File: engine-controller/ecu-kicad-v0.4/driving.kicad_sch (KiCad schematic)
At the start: 94 parts, among them U1 MCP1416, U10 RQ3E100, U11 MCP1416, U12 RQ3E100, U13 MCP1416, U14 MCP1416, U15 RQ3E100, U16 RQ3E100, U17 MCP1416, U18 MCP1416, U19 MCP1416, U20 MCP1416, U21 RQ3E100, U22 RQ3E100, U23 RQ3E100, U24 RQ3E100, U25 MCP1416, U26 MCP1416, U27 RQ3E100, U28 RQ3E100, U29 MCP1416, U30 MCP1416, U4 MCP1416, U5 MCP1416, U51 RQ3E100, U52 MCP1416, U53 RQ3E100, U54 MCP1416, U55 RQ3E100, U56 MCP1416, U57 RQ3E100, U58 MCP1416, U6 RQ3E100, U7 MCP1416, U8 RQ3E100, U9 MCP1416

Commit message: That's a lot of changes
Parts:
- added C74, C75, C76, C77: 1uF, Capacitor_SMD:C_0402_1005Metric, symbol Device:C_Small
- added R57, R58, R59, R60: 20K, symbol Device:R_Small
- added U59, U60, U61, U62: MCP1416, Package_TO_SOT_SMD:SOT-23-5, symbol Driver_FET:MCP1416
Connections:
- net +5V: now also C74.2, C75.2, C76.2, C77.2, U59.2 (Vdd), U60.2 (Vdd), U61.2 (Vdd), U62.2 (Vdd)
- net GND: now also C74.1, C75.1, C76.1, C77.1, R57.1, R58.1, R59.1, R60.1, U59.4 (GND), U60.4 (GND), U61.4 (GND), U62.4 (GND)
- new net PWM_CTRL4: R57.2, U59.3 (IN)
- new net PWM_CTRL5: R58.2, U60.3 (IN)
- new net PWM_CTRL6: R59.2, U61.3 (IN)
- new net PWM_CTRL7: R60.2, U62.3 (IN)
- new net PWM_OUT4: U59.5 (OUT)
- new net PWM_OUT5: U60.5 (OUT)
- new net PWM_OUT6: U61.5 (OUT)
- new net PWM_OUT7: U62.5 (OUT)
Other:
- moved on the sheet: C1, C10, C11, C12, C13, C2, C3, C37, C38, C39, C4, C5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

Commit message: Changed ECU v0.4 to use more fused outputs
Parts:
- removed C11, C12, C13, C37, C72, C73: 1uF, Capacitor_SMD:C_0402_1005Metric, symbol Device:C_Small
- removed D10, D11, D12, D15, D16, D9: GS1G, Diode_SMD:D_SMA, symbol Device:D_Small
- removed R11, R12, R13, R14, R55, R56: 20K, symbol Device:R_Small
- removed U19, U20, U25, U26, U56, U58: MCP1416, Package_TO_SOT_SMD:SOT-23-5, symbol Driver_FET:MCP1416
- removed U23, U24, U27, U28, U55, U57: RQ3E100, CustomFootprints:HSMT-8, symbol CustomSymbols:RQ3E100
- added C94, C95, C96, C97, C98, C99: 1uF, Capacitor_SMD:C_0402_1005Metric, symbol Device:C_Small
- added D17, D18, D19, D20, D21, D22: GS1G, Diode_SMD:D_SMA, symbol Device:D_Small
- added F3, F4, F5, F6, F7, F8: SF-2410F-T, CustomFootprints:SF-2410F-T, symbol Device:Fuse_Small
- added R20, R39, R40, R48, R49, R50: 20K, symbol Device:R_Small
- added U34, U37, U47, U48, U49, U50: MCP1416, Package_TO_SOT_SMD:SOT-23-5, symbol Driver_FET:MCP1416
- added U38, U46, U63, U64, U65, U66: RQ3E100, CustomFootprints:HSMT-8, symbol CustomSymbols:RQ3E100
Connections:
- net +12V: now also C94.2, C95.2, C96.2, C97.2, C98.2, C99.2, U34.2 (Vdd), U37.2 (Vdd), U47.2 (Vdd), U48.2 (Vdd), U49.2 (Vdd), U50.2 (Vdd)
- net GND: now also C94.1, C95.1, C96.1, C97.1, C98.1, C99.1, R20.1, R39.1, R40.1, R48.1, R49.1, R50.1, U34.4 (GND), U37.4 (GND), U38.1 (Source), U38.2 (Source), U38.3 (Source), U46.1 (Source), U46.2 (Source), U46.3 (Source), U47.4 (GND), U48.4 (GND), U49.4 (GND), U50.4 (GND), U63.1 (Source), U63.2 (Source), U63.3 (Source), U64.1 (Source), U64.2 (Source), U64.3 (Source), U65.1 (Source), U65.2 (Source), U65.3 (Source), U66.1 (Source), U66.2 (Source), U66.3 (Source)
- net Vdrive: now also D17.1 (K), D18.1 (K), D19.1 (K), D20.1 (K), D21.1 (K), D22.1 (K)
- net OUT_AUX0 renamed OUT_FUSED0
- net OUT_AUX1 renamed OUT_FUSED1
- net OUT_AUX_CTRL0 renamed OUT_FUSED_CTRL0
- net OUT_AUX_CTRL1 renamed OUT_FUSED_CTRL1
- net OUT_FUSED_CTRL1: now also R20.2, U34.3 (IN)
- new net: F5.1, U63.5 (Drain), U63.6 (Drain), U63.7 (Drain), U63.8 (Drain)
- new net: U47.5 (OUT), U63.4 (Gate)
- new net: U34.5 (OUT), U38.4 (Gate)
- new net: F3.1, U38.5 (Drain), U38.6 (Drain), U38.7 (Drain), U38.8 (Drain)
- new net: U49.5 (OUT), U65.4 (Gate)
- new net: F7.1, U65.5 (Drain), U65.6 (Drain), U65.7 (Drain), U65.8 (Drain)
- new net: F6.1, U64.5 (Drain), U64.6 (Drain), U64.7 (Drain), U64.8 (Drain)
- new net: U48.5 (OUT), U64.4 (Gate)
- new net: U50.5 (OUT), U66.4 (Gate)
- new net: F8.1, U66.5 (Drain), U66.6 (Drain), U66.7 (Drain), U66.8 (Drain)
- new net: F4.1, U46.5 (Drain), U46.6 (Drain), U46.7 (Drain), U46.8 (Drain)
- new net: U37.5 (OUT), U46.4 (Gate)
- new net OUT_FUSED2: D17.2 (A), F3.2
- new net OUT_FUSED3: D18.2 (A), F4.2
- new net OUT_FUSED4: D19.2 (A), F5.2
- new net OUT_FUSED5: D20.2 (A), F6.2
- new net OUT_FUSED6: D21.2 (A), F7.2
- new net OUT_FUSED7: D22.2 (A), F8.2
- new net OUT_FUSED_CTRL3: R39.2, U37.3 (IN)
- new net OUT_FUSED_CTRL4: R40.2, U47.3 (IN)
- new net OUT_FUSED_CTRL5: R48.2, U48.3 (IN)
- new net OUT_FUSED_CTRL6: R49.2, U49.3 (IN)
- new net OUT_FUSED_CTRL7: R50.2, U50.3 (IN)
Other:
- moved on the sheet: C3, C4, D1, D2, F1, F2, R3, R4, U5, U6, U7, U8

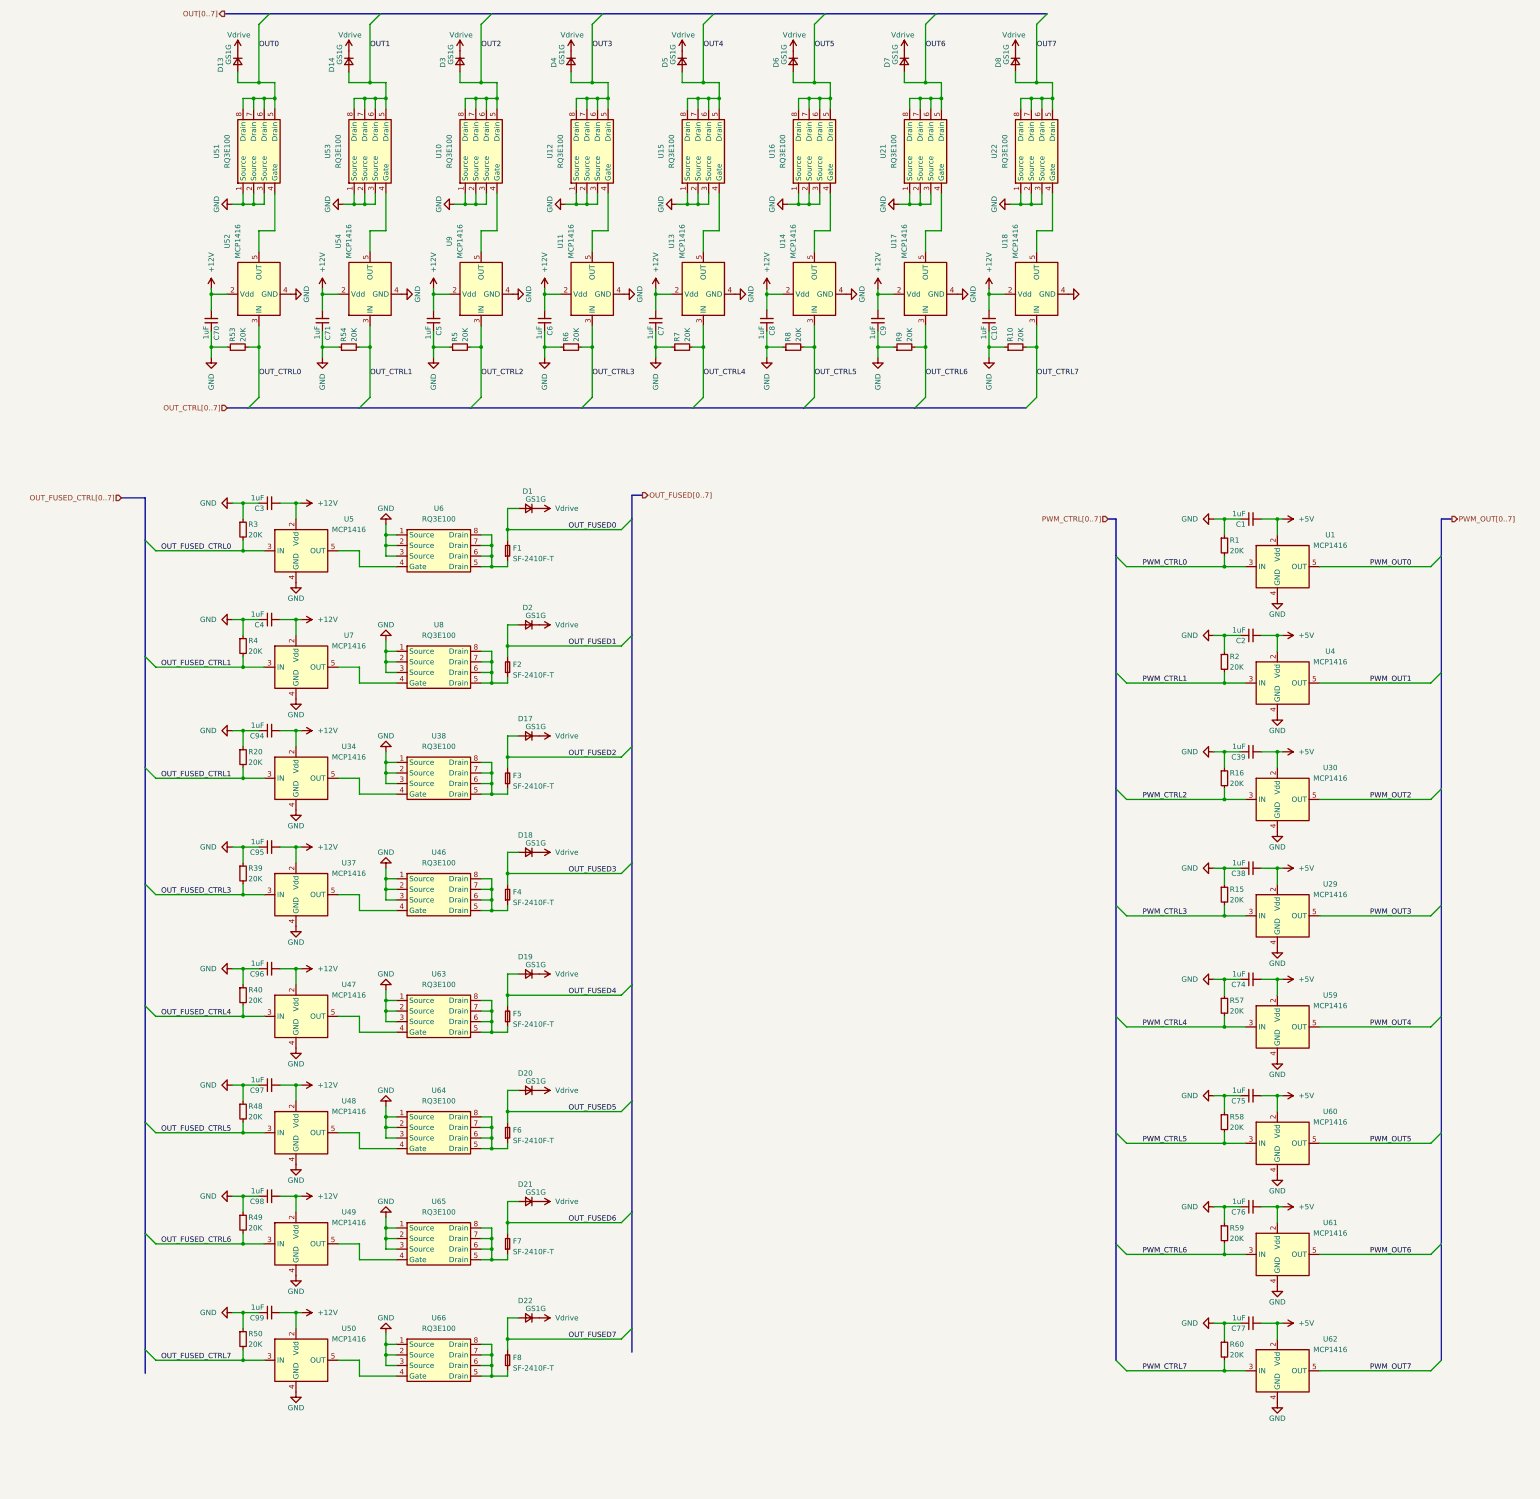
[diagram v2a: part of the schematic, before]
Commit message: Better sim configs + ecu v0.4 work
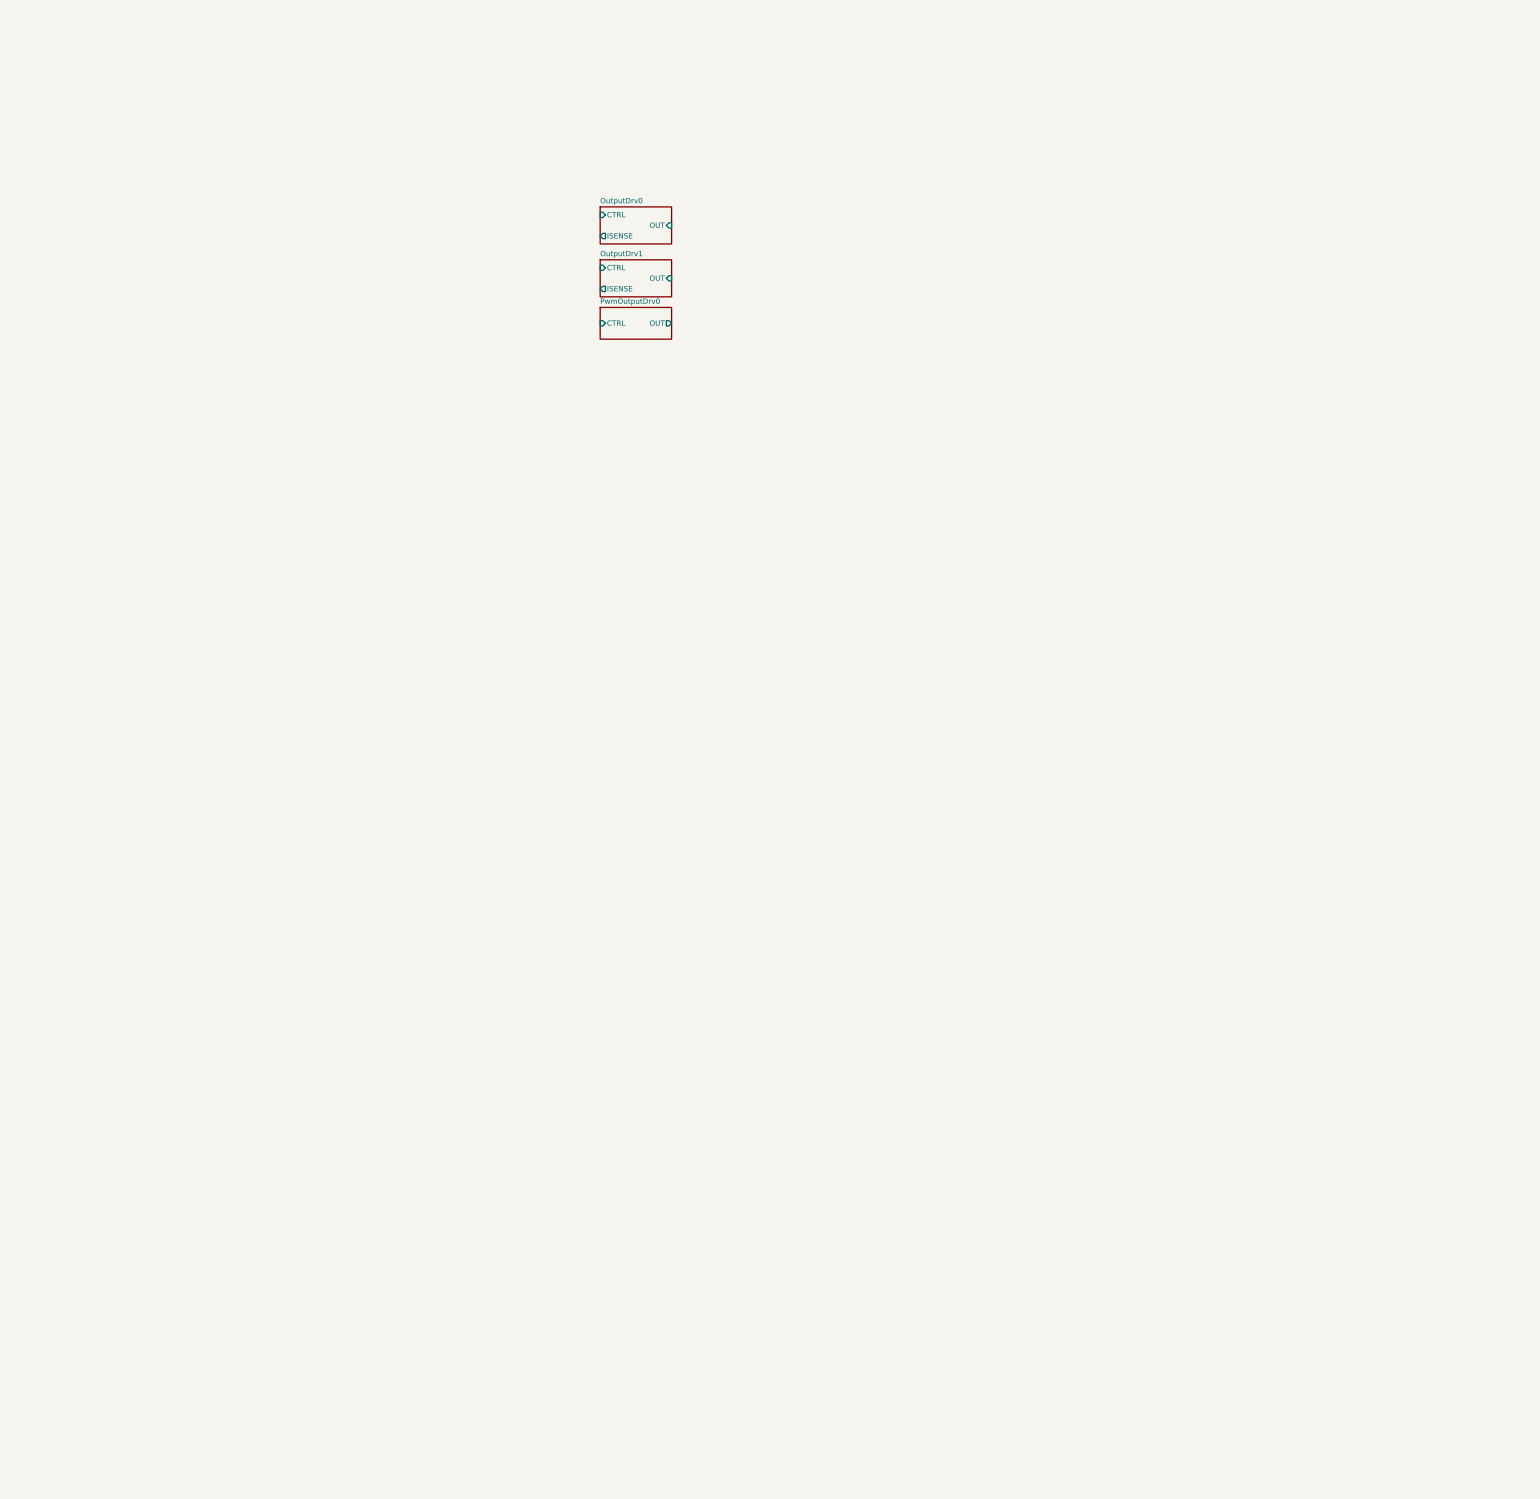
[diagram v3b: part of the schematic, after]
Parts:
- removed C1, C10, C2, C3, C38, C39, C4, C5, C6, C7, C70, C71, C74, C75, C76, C77, C8, C9, C94, C95, C96, C97, C98, C99: 1uF, Capacitor_SMD:C_0402_1005Metric, symbol Device:C_Small
- removed D1, D13, D14, D17, D18, D19, D2, D20, D21, D22, D3, D4, D5, D6, D7, D8: GS1G, Diode_SMD:D_SMA, symbol Device:D_Small
- removed F1, F2, F3, F4, F5, F6, F7, F8: SF-2410F-T, CustomFootprints:SF-2410F-T, symbol Device:Fuse_Small
- removed R1, R10, R15, R16, R2, R20, R3, R39, R4, R40, R48, R49, R5, R50, R53, R54, R57, R58, R59, R6, R60, R7, R8, R9: 20K, symbol Device:R_Small
- removed U1, U11, U13, U14, U17, U18, U29, U30, U34, U37, U4, U47, U48, U49, U5, U50, U52, U54, U59, U60, U61, U62, U7, U9: MCP1416, Package_TO_SOT_SMD:SOT-23-5, symbol Driver_FET:MCP1416
- removed U10, U12, U15, U16, U21, U22, U38, U46, U51, U53, U6, U63, U64, U65, U66, U8: RQ3E100, CustomFootprints:HSMT-8, symbol CustomSymbols:RQ3E100
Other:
- added sheet OutputDrv0 (output_drv.kicad_sch)
- added sheet OutputDrv1 (output_drv.kicad_sch)
- added sheet PwmOutputDrv0 (pwm_output_drv.kicad_sch)

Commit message: Progress on ECU v0.4
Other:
- added sheet PwmOutputDrv1 (pwm_output_drv.kicad_sch)
- added sheet PwmOutputDrv2 (pwm_output_drv.kicad_sch)
- added sheet PwmOutputDrv3 (pwm_output_drv.kicad_sch)
- added sheet PwmOutputDrv4 (pwm_output_drv.kicad_sch)
- added sheet PwmOutputDrv5 (pwm_output_drv.kicad_sch)
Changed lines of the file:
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@@
     (effects (font (size 1.27 1.27)) (justify left bottom))
   )
-  (sheet (at 168.275 99.06) (size 17.145 8.89) (fields_autoplaced)
+  (sheet (at 170.18 68.58) (size 17.78 7.62) (fields_autoplaced)
     (stroke (width 0.1524) (type solid))
     (fill (color 0 0 0 0.0000))
-    (property "Sheetname" "OutputDrv1" (at 168.275 98.3484 0)
+    (property "Sheetname" "PwmOutputDrv1" (at 170.18 67.8684 0)
       (effects (font (size 1.27 1.27)) (justify left bottom))
     )
-    (property "Sheetfile" "output_drv.kicad_sch" (at 168.275 108.5346 0)
+    (property "Sheetfile" "pwm_output_drv.kicad_sch" (at 170.18 76.7846 0)
       (effects (font (size 1.27 1.27)) (justify left top) hide)
     )
-    (pin "OUT" input (at 185.42 103.505 0)
+    (pin "OUT" output (at 187.96 72.39 0)
       (effects (font (size 1.27 1.27)) (justify right))
     )
-    (pin "CTRL" input (at 168.275 100.965 180)
+    (pin "CTRL" input (at 170.18 72.39 180)
       (effects (font (size 1.27 1.27)) (justify left))
     )
-    (pin "ISENSE" output (at 168.275 106.045 180)
+    (instances
+      (project "ecu-kicad-v0.4"
+        (path "/36cc65d2-4dd3-4f51-bcce-4252e60c9ae8/786c8415-1305-4598-963d-843f7f154a96" (page "21"))
+      )
+    )
+  )
+  (sheet (at 170.18 91.44) (size 17.78 7.62) (fields_autoplaced)
+    (stroke (width 0.1524) (type solid))
+    (fill (color 0 0 0 0.0000))
+    (property "Sheetname" "PwmOutputDrv3" (at 170.18 90.7284 0)
+      (effects (font (size 1.27 1.27)) (justify left bottom))
+    )
+    (property "Sheetfile" "pwm_output_drv.kicad_sch" (at 170.18 99.6446 0)
+      (effects (font (size 1.27 1.27)) (justify left top) hide)
+    )
+    (pin "OUT" output (at 187.96 95.25 0)
+      (effects (font (size 1.27 1.27)) (justify right))
+    )
+    (pin "CTRL" input (at 170.18 95.25 180)
+      (effects (font (size 1.27 1.27)) (justify left))
+    )
+    (instances
+      (project "ecu-kicad-v0.4"
+        (path "/36cc65d2-4dd3-4f51-bcce-4252e60c9ae8/786c8415-1305-4598-963d-843f7f154a96" (page "23"))
+      )
+    )
+  )
+  (sheet (at 170.18 102.87) (size 17.78 7.62) (fields_autoplaced)
+    (stroke (width 0.1524) (type solid))
+    (fill (color 0 0 0 0.0000))
+    (property "Sheetname" "PwmOutputDrv4" (at 170.18 102.1584 0)
+      (effects (font (size 1.27 1.27)) (justify left bottom))
+    )
+    (property "Sheetfile" "pwm_output_drv.kicad_sch" (at 170.18 111.0746 0)
+      (effects (font (size 1.27 1.27)) (justify left top) hide)
+    )
+    (pin "OUT" output (at 187.96 106.68 0)
+      (effects (font (size 1.27 1.27)) (justify right))
+    )
+    (pin "CTRL" input (at 170.18 106.68 180)
+      (effects (font (size 1.27 1.27)) (justify left))
+    )
+    (instances
+      (project "ecu-kicad-v0.4"
+        (path "/36cc65d2-4dd3-4f51-bcce-4252e60c9ae8/786c8415-1305-4598-963d-843f7f154a96" (page "24"))
+      )
+    )
+  )
+  (sheet (at 78.105 79.375) (size 16.51 8.89) (fields_autoplaced)
+    (stroke (width 0.1524) (type solid))
+    (fill (color 0 0 0 0.0000))
+    (property "Sheetname" "OutputDrv1" (at 78.105 78.6634 0)
+      (effects (font (size 1.27 1.27)) (justify left bottom))
+    )
+    (property "Sheetfile" "output_drv.kicad_sch" (at 78.105 88.8496 0)
+      (effects (font (size 1.27 1.27)) (justify left top) hide)
+    )
+    (pin "OUT" input (at 95.25 83.82 0)
+      (effects (font (size 1.27 1.27)) (justify right))
+    )
+    (pin "CTRL" input (at 78.105 81.28 180)
+      (effects (font (size 1.27 1.27)) (justify left))
+    )
+    (pin "ISENSE" output (at 78.105 86.36 180)
       (effects (font (size 1.27 1.27)) (justify left))
     )
@@
     )
   )
-  (sheet (at 168.275 86.36) (size 17.145 8.89) (fields_autoplaced)
+  (sheet (at 170.18 80.01) (size 17.78 7.62) (fields_autoplaced)
     (stroke (width 0.1524) (type solid))
     (fill (color 0 0 0 0.0000))
-    (property "Sheetname" "OutputDrv0" (at 168.275 85.6484 0)
+    (property "Sheetname" "PwmOutputDrv2" (at 170.18 79.2984 0)
       (effects (font (size 1.27 1.27)) (justify left bottom))
     )
-    (property "Sheetfile" "output_drv.kicad_sch" (at 168.275 95.8346 0)
+    (property "Sheetfile" "pwm_output_drv.kicad_sch" (at 170.18 88.2146 0)
       (effects (font (size 1.27 1.27)) (justify left top) hide)
     )
-    (pin "OUT" input (at 185.42 90.805 0)
+    (pin "OUT" output (at 187.96 83.82 0)
       (effects (font (size 1.27 1.27)) (justify right))
     )
-    (pin "CTRL" input (at 168.275 88.265 180)
+    (pin "CTRL" input (at 170.18 83.82 180)
       (effects (font (size 1.27 1.27)) (justify left))
     )
-    (pin "ISENSE" output (at 168.275 93.345 180)
+    (instances
+      (project "ecu-kicad-v0.4"
+        (path "/36cc65d2-4dd3-4f51-bcce-4252e60c9ae8/786c8415-1305-4598-963d-843f7f154a96" (page "22"))
+      )
+    )
+  )
+  (sheet (at 78.105 66.675) (size 16.51 8.89) (fields_autoplaced)
+    (stroke (width 0.1524) (type solid))
+    (fill (color 0 0 0 0.0000))
+    (property "Sheetname" "OutputDrv0" (at 78.105 65.9634 0)
+      (effects (font (size 1.27 1.27)) (justify left bottom))
+    )
+    (property "Sheetfile" "output_drv.kicad_sch" (at 78.105 76.1496 0)
+      (effects (font (size 1.27 1.27)) (justify left top) hide)
+    )
+    (pin "OUT" input (at 95.25 71.12 0)
+      (effects (font (size 1.27 1.27)) (justify right))
+    )
+    (pin "CTRL" input (at 78.105 68.58 180)
+      (effects (font (size 1.27 1.27)) (justify left))
+    )
+    (pin "ISENSE" output (at 78.105 73.66 180)
       (effects (font (size 1.27 1.27)) (justify left))
     )
@@
     )
   )
-  (sheet (at 168.275 110.49) (size 17.145 7.62) (fields_autoplaced)
+  (sheet (at 170.18 114.3) (size 17.78 7.62) (fields_autoplaced)
     (stroke (width 0.1524) (type solid))
     (fill (color 0 0 0 0.0000))
-    (property "Sheetname" "PwmOutputDrv0" (at 168.275 109.7784 0)
+    (property "Sheetname" "PwmOutputDrv5" (at 170.18 113.5884 0)
       (effects (font (size 1.27 1.27)) (justify left bottom))
     )
-    (property "Sheetfile" "pwm_output_drv.kicad_sch" (at 168.275 118.6946 0)
+    (property "Sheetfile" "pwm_output_drv.kicad_sch" (at 170.18 122.5046 0)
       (effects (font (size 1.27 1.27)) (justify left top) hide)
     )
-    (pin "OUT" output (at 185.42 114.3 0)
+    (pin "OUT" output (at 187.96 118.11 0)
       (effects (font (size 1.27 1.27)) (justify right))
     )
-    (pin "CTRL" input (at 168.275 114.3 180)
+    (pin "CTRL" input (at 170.18 118.11 180)
       (effects (font (size 1.27 1.27)) (justify left))
     )
+    (instances
+      (project "ecu-kicad-v0.4"
+        (path "/36cc65d2-4dd3-4f51-bcce-4252e60c9ae8/786c8415-1305-4598-963d-843f7f154a96" (page "25"))
+      )
+    )
+  )
+  (sheet (at 170.18 57.15) (size 17.78 7.62) (fields_autoplaced)
+    (stroke (width 0.1524) (type solid))
+    (fill (color 0 0 0 0.0000))
+    (property "Sheetname" "PwmOutputDrv0" (at 170.18 56.4384 0)
+      (effects (font (size 1.27 1.27)) (justify left bottom))
+    )
+    (property "Sheetfile" "pwm_output_drv.kicad_sch" (at 170.18 65.3546 0)
+      (effects (font (size 1.27 1.27)) (justify left top) hide)
+    )
+    (pin "OUT" output (at 187.96 60.96 0)
+      (effects (font (size 1.27 1.27)) (justify right))
+    )
+    (pin "CTRL" input (at 170.18 60.96 180)
+      (effects (font (size 1.27 1.27)) (justify left))
+    )
